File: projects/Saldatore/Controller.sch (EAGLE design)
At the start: 20 parts, among them U1 ATTINY85-P, X1 SMKDSP_1,5/2

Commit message: in lavoro saldatore.
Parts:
- R4: value 47-2W -> 120-5W
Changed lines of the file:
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@@
 <part name="GND11" library="supply1" library_urn="urn:adsk.eagle:library:371" deviceset="GND" device=""/>
 <part name="D2" library="diode_MOD" deviceset="ZENER-DIODE" device="DO41Z10" package3d_urn="urn:adsk.eagle:package:43341/1" value="5v1-1W"/>
-<part name="R4" library="rcl" library_urn="urn:adsk.eagle:library:334" deviceset="R-EU_" device="0204/7" package3d_urn="urn:adsk.eagle:package:23498/2" value="47-2W"/>
+<part name="R4" library="rcl" library_urn="urn:adsk.eagle:library:334" deviceset="R-EU_" device="0204/7" package3d_urn="urn:adsk.eagle:package:23498/2" value="120-5W"/>
 <part name="SOLDERING" library="con-lstb" library_urn="urn:adsk.eagle:library:162" deviceset="MA05-1" device="" package3d_urn="urn:adsk.eagle:package:8332/1"/>
 <part name="U1" library="_hhn_attiny25_45_85" deviceset="ATTINY85*" device="P" technology="-"/>

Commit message: aggiornato saldatore.
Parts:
- removed D2: 5v1-1W, diode_MOD:ZENER-DIODEDO41Z10
- removed R4: 120-5W, rcl:R-EU_0204/7
- added C1: 0.1u, rcl:C-EU025-025X050
- added C2: 1u, rcl:C-EU025-025X050
- added LM317: (no value), v-reg:LM317TS
- added R10: 240, rcl:R-EU_0204/7
- added R12: 1k, rcl:R-TRIMM64W
- R1: value 270 -> 220
- R8: value 10K -> 1k
- renumbered LM358 to LM258
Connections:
- new net N$67: LM317.ADJ, R10.1, R12.A
- net 24V: now also C1.2, LM317.IN; no longer R4.2
- net GND: now also C1.1, C2.1, R12.E, R12.S; no longer D2.A
- net VCC: now also C2.2, LM317.OUT, R10.2; no longer D2.C, R4.1

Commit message: in lavoro immagine scheda controller.
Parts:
- LM258: value LM358N -> LM258N
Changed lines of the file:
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@@
 <part name="R8" library="rcl" library_urn="urn:adsk.eagle:library:334" deviceset="R-EU_" device="0204/7" package3d_urn="urn:adsk.eagle:package:23498/2" value="1k"/>
 <part name="R5" library="rcl" library_urn="urn:adsk.eagle:library:334" deviceset="R-EU_" device="0204/7" package3d_urn="urn:adsk.eagle:package:23498/2" value="1k"/>
-<part name="LM258" library="linear" library_urn="urn:adsk.eagle:library:262" deviceset="LM2903" device="N" package3d_urn="urn:adsk.eagle:package:16409/2" value="LM358N"/>
+<part name="LM258" library="linear" library_urn="urn:adsk.eagle:library:262" deviceset="LM2903" device="N" package3d_urn="urn:adsk.eagle:package:16409/2" value="LM258N"/>
 <part name="GND2" library="supply1" library_urn="urn:adsk.eagle:library:371" deviceset="GND" device=""/>
 <part name="GND3" library="supply1" library_urn="urn:adsk.eagle:library:371" deviceset="GND" device=""/>

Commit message: aggiornato controller
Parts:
- removed LED1: (no value), led:LED3MM
- added LED: (no value), jumper:JP1E
- U1: value ATTINY85-P -> ATTINY85
- renumbered JP1 to RST, PROGRAMMER to PROG, SOLDERING to SOLD, TRIMM_100K to T_100K
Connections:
- net GND: now also LED.2; no longer LED1.C
- net N$61: now also LED.1; no longer LED1.A

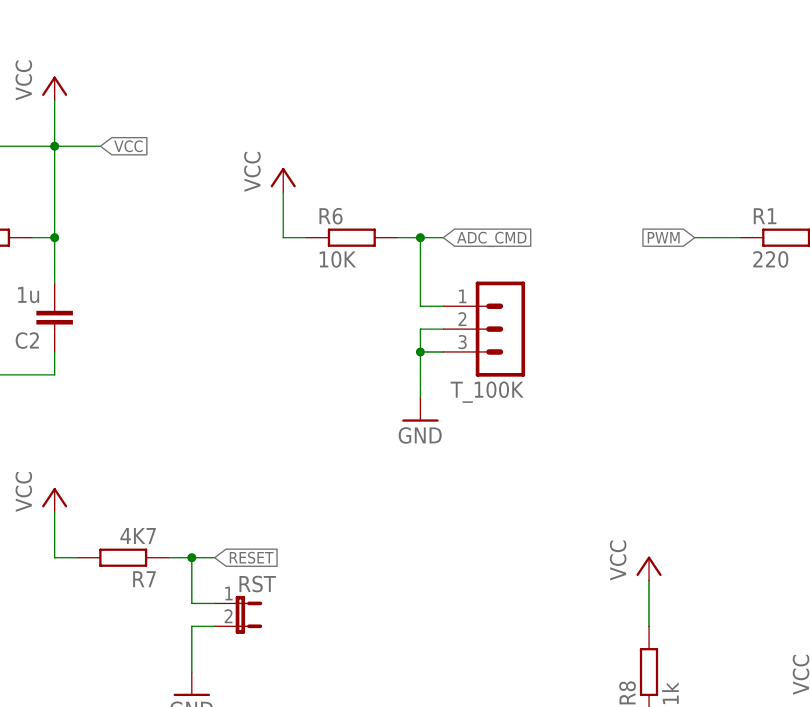
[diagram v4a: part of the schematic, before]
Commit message: aggiornata configurazione potenziometro di comando.
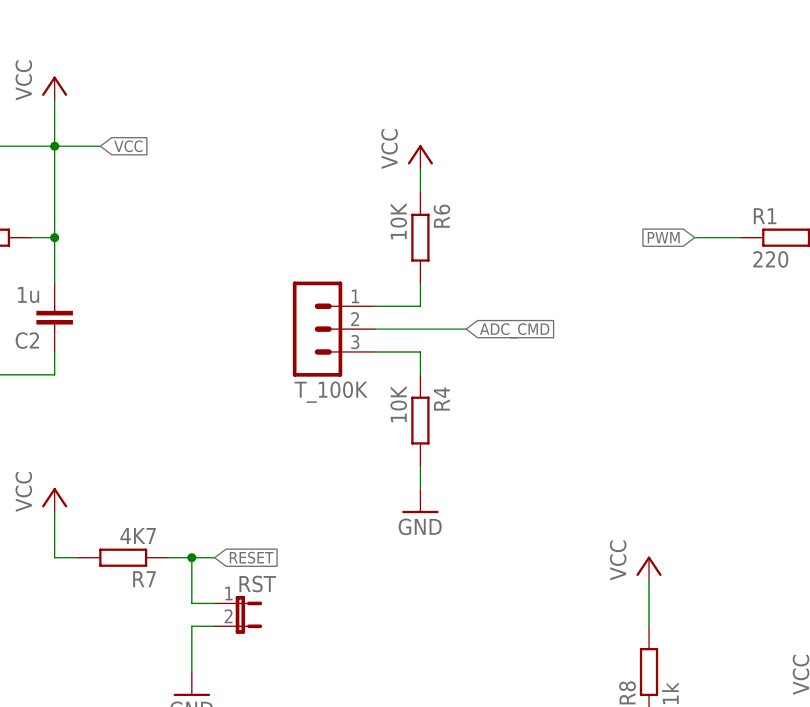
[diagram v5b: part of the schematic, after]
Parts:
- added R4: 10K, rcl:R-EU_0204/2V
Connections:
- new net N$72: R4.1, T_100K.3
- net ADC_CMD: now also T_100K.2
- net GND: now also R4.2; no longer T_100K.2, T_100K.3
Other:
- moved on the sheet: R6, T_100K
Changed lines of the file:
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@@
 <?xml version="1.0" encoding="utf-8"?>
 <!DOCTYPE eagle SYSTEM "eagle.dtd">
-<eagle version="9.5.2">
+<eagle version="9.5.1">
 <drawing>
 <settings>
@@
 <part name="GND1" library="supply1" library_urn="urn:adsk.eagle:library:371" deviceset="GND" device=""/>
 <part name="LED" library="jumper" library_urn="urn:adsk.eagle:library:252" deviceset="JP1E" device="" package3d_urn="urn:adsk.eagle:package:15455/1"/>
+<part name="R4" library="rcl" library_urn="urn:adsk.eagle:library:334" deviceset="R-EU_" device="0204/2V" package3d_urn="urn:adsk.eagle:package:23495/1" value="10K"/>
 </parts>
 <sheets>
@@
 <attribute name="NAME" x="95.25" y="-11.049" size="1.778" layer="95"/>
 </instance>
-<instance part="R6" gate="G$1" x="-5.08" y="33.02" smashed="yes">
-<attribute name="NAME" x="-8.89" y="34.5186" size="1.778" layer="95"/>
-<attribute name="VALUE" x="-8.89" y="29.718" size="1.778" layer="96"/>
-</instance>
-<instance part="T_100K" gate="G$1" x="12.7" y="22.86" smashed="yes" rot="R180">
-<attribute name="VALUE" x="13.97" y="30.48" size="1.778" layer="96" rot="R180"/>
-<attribute name="NAME" x="13.97" y="17.018" size="1.778" layer="95" rot="R180"/>
-</instance>
-<instance part="GND4" gate="1" x="2.54" y="12.7" smashed="yes">
-<attribute name="VALUE" x="0" y="10.16" size="1.778" layer="96"/>
+<instance part="R6" gate="G$1" x="2.54" y="33.02" smashed="yes" rot="R270">
+<attribute name="NAME" x="4.0386" y="36.83" size="1.778" layer="95" rot="R270"/>
+<attribute name="VALUE" x="-0.762" y="36.83" size="1.778" layer="96" rot="R270"/>
+</instance>
+<instance part="T_100K" gate="G$1" x="-10.16" y="22.86" smashed="yes" rot="MR180">
+<attribute name="VALUE" x="-11.43" y="30.48" size="1.778" layer="96" rot="MR180"/>
+<attribute name="NAME" x="-11.43" y="17.018" size="1.778" layer="95" rot="MR180"/>
+</instance>
+<instance part="GND4" gate="1" x="2.54" y="2.54" smashed="yes">
+<attribute name="VALUE" x="0" y="0" size="1.778" layer="96"/>
 </instance>
 <instance part="P+1" gate="VCC" x="-38.1" y="50.8" smashed="yes">
 <attribute name="VALUE" x="-40.64" y="48.26" size="1.778" layer="96" rot="R90"/>
 </instance>
-<instance part="P+2" gate="VCC" x="-12.7" y="40.64" smashed="yes">
-<attribute name="VALUE" x="-15.24" y="38.1" size="1.778" layer="96" rot="R90"/>
+<instance part="P+2" gate="VCC" x="2.54" y="43.18" smashed="yes">
+<attribute name="VALUE" x="0" y="40.64" size="1.778" layer="96" rot="R90"/>
 </instance>
 <instance part="P+3" gate="VCC" x="27.94" y="-2.54" smashed="yes">
@@
 <attribute name="NAME" x="111.76" y="-39.37" size="1.778" layer="95"/>
 <attribute name="VALUE" x="111.76" y="-46.355" size="1.778" layer="96"/>
+</instance>
+<instance part="R4" gate="G$1" x="2.54" y="12.7" smashed="yes" rot="R270">
+<attribute name="NAME" x="4.0386" y="16.51" size="1.778" layer="95" rot="R270"/>
+<attribute name="VALUE" x="-0.762" y="16.51" size="1.778" layer="96" rot="R270"/>
 </instance>
 </instances>
@@
 <wire x1="88.9" y1="-10.16" x2="86.36" y2="-10.16" width="0.1524" layer="91"/>
 <label x="86.36" y="-10.16" size="1.27" layer="95" rot="R180" xref="yes"/>
-</segment>
-<segment>
-<pinref part="T_100K" gate="G$1" pin="2"/>
-<wire x1="5.08" y1="22.86" x2="2.54" y2="22.86" width="0.1524" layer="91"/>
-<wire x1="2.54" y1="22.86" x2="2.54" y2="20.32" width="0.1524" layer="91"/>
-<pinref part="T_100K" gate="G$1" pin="3"/>
-<wire x1="2.54" y1="20.32" x2="5.08" y2="20.32" width="0.1524" layer="91"/>
-<wire x1="2.54" y1="20.32" x2="2.54" y2="15.24" width="0.1524" layer="91"/>
-<junction x="2.54" y="20.32"/>
-<pinref part="GND4" gate="1" pin="GND"/>
 </segment>
 <segment>
@@
 <wire x1="-38.1" y1="17.78" x2="-38.1" y2="20.32" width="0.1524" layer="91"/>
 </segment>
+<segment>
+<pinref part="GND4" gate="1" pin="GND"/>
+<pinref part="R4" gate="G$1" pin="2"/>
+<wire x1="2.54" y1="5.08" x2="2.54" y2="7.62" width="0.1524" layer="91"/>
+</segment>
 </net>
 <net name="N$1" class="0">
@@
 <segment>
 <pinref part="R6" gate="G$1" pin="2"/>
-<wire x1="0" y1="33.02" x2="2.54" y2="33.02" width="0.1524" layer="91"/>
-<wire x1="2.54" y1="33.02" x2="2.54" y2="25.4" width="0.1524" layer="91"/>
+<wire x1="2.54" y1="27.94" x2="2.54" y2="25.4" width="0.1524" layer="91"/>
 <pinref part="T_100K" gate="G$1" pin="1"/>
-<wire x1="2.54" y1="25.4" x2="5.08" y2="25.4" width="0.1524" layer="91"/>
-<wire x1="2.54" y1="33.02" x2="5.08" y2="33.02" width="0.1524" layer="91"/>
-<junction x="2.54" y="33.02"/>
-<label x="5.08" y="33.02" size="1.27" layer="95" xref="yes"/>
+<wire x1="2.54" y1="25.4" x2="-2.54" y2="25.4" width="0.1524" layer="91"/>
 </segment>
 <segment>
@@
 <wire x1="114.3" y1="12.7" x2="114.3" y2="10.16" width="0.1524" layer="91"/>
 <label x="114.3" y="10.16" size="1.27" layer="95" rot="R270" xref="yes"/>
+</segment>
+<segment>
+<pinref part="T_100K" gate="G$1" pin="2"/>
+<label x="7.62" y="22.86" size="1.27" layer="95" xref="yes"/>
+<wire x1="-2.54" y1="22.86" x2="7.62" y2="22.86" width="0.1524" layer="91"/>
 </segment>
 </net>
@@
 <segment>
 <pinref part="R6" gate="G$1" pin="1"/>
-<wire x1="-10.16" y1="33.02" x2="-12.7" y2="33.02" width="0.1524" layer="91"/>
 <pinref part="P+2" gate="VCC" pin="VCC"/>
-<wire x1="-12.7" y1="38.1" x2="-12.7" y2="33.02" width="0.1524" layer="91"/>
+<wire x1="2.54" y1="40.64" x2="2.54" y2="38.1" width="0.1524" layer="91"/>
 </segment>
 <segment>
@@
 </segment>
 </net>
+<net name="N$72" class="0">
+<segment>
+<pinref part="T_100K" gate="G$1" pin="3"/>
+<wire x1="2.54" y1="20.32" x2="-2.54" y2="20.32" width="0.1524" layer="91"/>
+<pinref part="R4" gate="G$1" pin="1"/>
+<wire x1="2.54" y1="17.78" x2="2.54" y2="20.32" width="0.1524" layer="91"/>
+</segment>
+</net>
